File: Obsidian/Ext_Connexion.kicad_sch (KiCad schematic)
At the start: 36 parts, among them J4 Conn_02x20_Odd_Even

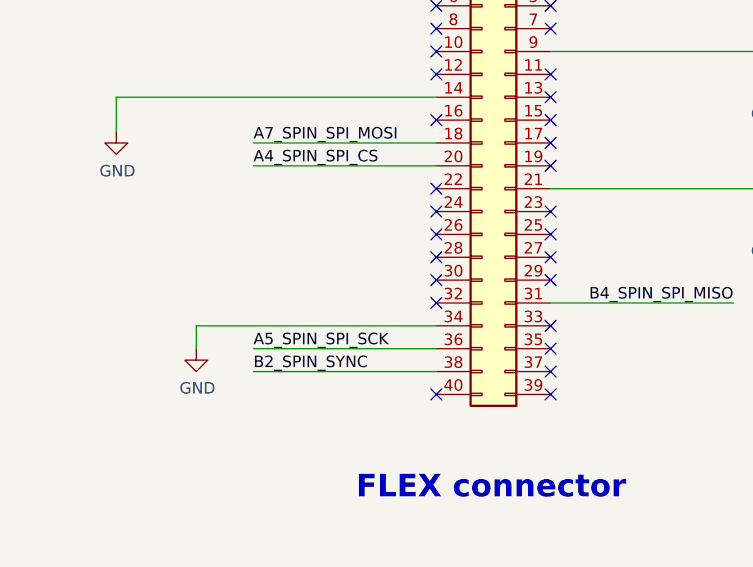
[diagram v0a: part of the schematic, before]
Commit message: moving flex pins for SCIN and SCK from PA13/PA14 to PC8/PC9
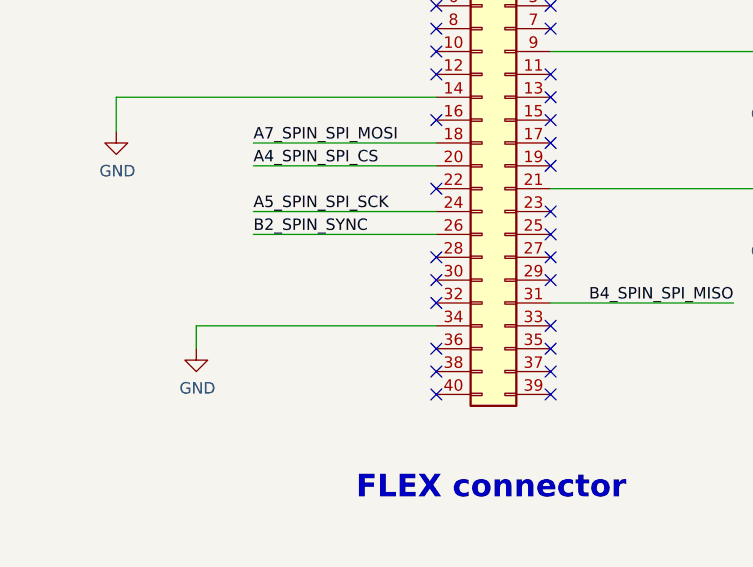
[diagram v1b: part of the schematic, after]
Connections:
- net A5_SPIN_SPI_SCK: now also J4.24 (Pin_24); no longer J4.36 (Pin_36)
- net B2_SPIN_SYNC: now also J4.26 (Pin_26); no longer J4.38 (Pin_38)
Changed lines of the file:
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@@
 	)
 	(no_connect
-		(at 58.42 153.67)
+		(at 58.42 168.91)
 	)
 	(no_connect
@@
 	)
 	(no_connect
-		(at 58.42 156.21)
-	)
-	(no_connect
 		(at 71.12 146.05)
 	)
@@
 	(no_connect
 		(at 71.12 130.81)
+	)
+	(no_connect
+		(at 58.42 171.45)
 	)
 	(no_connect
@@
 	(wire
 		(pts
-			(xy 38.1 168.91) (xy 58.42 168.91)
-		)
-		(stroke
-			(width 0)
-			(type default)
-		)
-	)
-	(wire
-		(pts
 			(xy 33.02 63.5) (xy 54.61 63.5)
 		)
@@
 	(wire
 		(pts
+			(xy 38.1 153.67) (xy 58.42 153.67)
+		)
+		(stroke
+			(width 0)
+			(type default)
+		)
+	)
+	(wire
+		(pts
 			(xy 142.24 44.45) (xy 160.02 44.45)
 		)
@@
 		(pts
 			(xy 38.1 146.05) (xy 58.42 146.05)
-		)
-		(stroke
-			(width 0)
-			(type default)
-		)
-	)
-	(wire
-		(pts
-			(xy 38.1 171.45) (xy 58.42 171.45)
 		)
 		(stroke
@@
 	(wire
 		(pts
+			(xy 38.1 156.21) (xy 58.42 156.21)
+		)
+		(stroke
+			(width 0)
+			(type default)
+		)
+	)
+	(wire
+		(pts
 			(xy 185.42 44.45) (xy 191.77 44.45)
 		)
@@
 		)
 	)
+	(label "A5_SPIN_SPI_SCK"
+		(at 38.1 153.67 0)
+		(effects
+			(font
+				(size 1.27 1.27)
+			)
+			(justify left bottom)
+		)
+	)
 	(label "ARDUINO_D13"
 		(at 146.05 72.39 0)
@@
 		)
 	)
+	(label "B2_SPIN_SYNC"
+		(at 38.1 156.21 0)
+		(effects
+			(font
+				(size 1.27 1.27)
+			)
+			(justify left bottom)
+		)
+	)
 	(label "{SPIN}"
 		(at 109.22 41.91 180)
@@
 		)
 	)
-	(label "B2_SPIN_SYNC"
-		(at 38.1 171.45 0)
-		(effects
-			(font
-				(size 1.27 1.27)
-			)
-			(justify left bottom)
-		)
-	)
 	(label "ARDUINO_D5"
 		(at 146.05 52.07 0)
@@
 		)
 	)
-	(label "A5_SPIN_SPI_SCK"
-		(at 38.1 168.91 0)
-		(effects
-			(font
-				(size 1.27 1.27)
-			)
-			(justify left bottom)
-		)
-	)

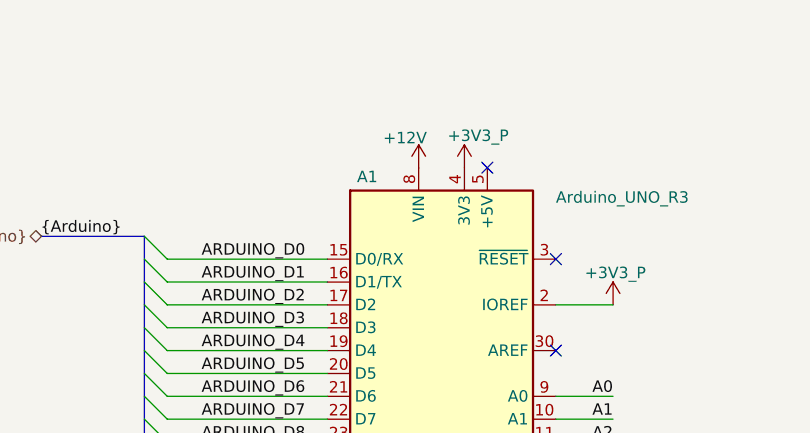
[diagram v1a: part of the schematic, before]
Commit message: correcting straightness of kicad plane around 1V2 regulator
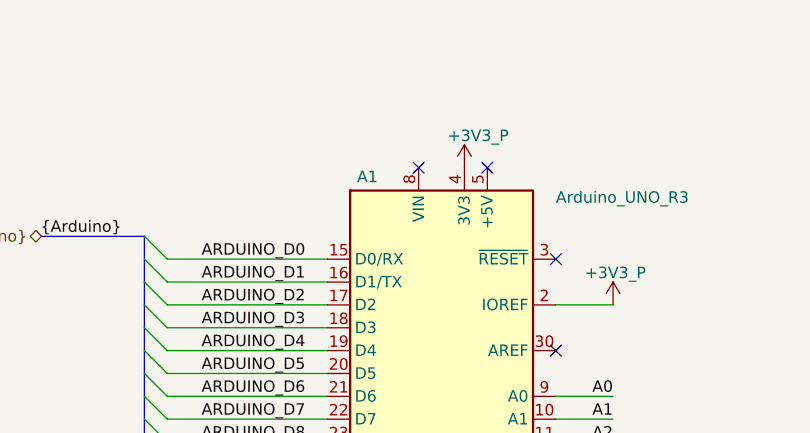
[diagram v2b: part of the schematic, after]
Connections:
- net +12V: no longer names the net of A1.8 (VIN)
- no-connect marks 34 -> 35
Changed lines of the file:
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@@
 	)
 	(no_connect
+		(at 170.18 29.21)
+	)
+	(no_connect
 		(at 71.12 140.97)
 	)
@@
 					(unit 1)
 				)
-			)
-		)
-	)
-	(symbol
-		(lib_id "Library_Symbol:+12V")
-		(at 170.18 29.21 0)
-		(unit 1)
-		(exclude_from_sim no)
-		(in_bom yes)
-		(on_board yes)
-		(dnp no)
-		(property "Reference" "#PWR0295"
-			(at 170.18 33.02 0)
-			(effects
-				(font
-					(size 1.27 1.27)
-				)
-				(hide yes)
-			)
-		)
-		(property "Value" "+12V"
-			(at 168.656 25.908 0)
-			(effects
-				(font
-					(size 1.27 1.27)
-				)
-			)
-		)
-		(property "Footprint" ""
-			(at 170.18 29.21 0)
-			(effects
-				(font
-					(size 1.27 1.27)
-				)
-				(hide yes)
-			)
-		)
-		(property "Datasheet" ""
-			(at 170.18 29.21 0)
-			(effects
-				(font
-					(size 1.27 1.27)
-				)
-				(hide yes)
-			)
-		)
-		(property "Description" "Power symbol creates a global label with name \"+12V\""
-			(at 170.18 29.21 0)
-			(effects
-				(font
-					(size 1.27 1.27)
-				)
-				(hide yes)
-			)
-		)
-		(pin "1"
-		)
-		(instances
-			(project "Obsidian"
-				(path "/c2a4f786-b14c-434a-acf7-b20fb2221b0b/37c76a7d-e360-409e-9f8e-819f870af943"
-					(reference "#PWR0295")
-					(unit 1)
-				)

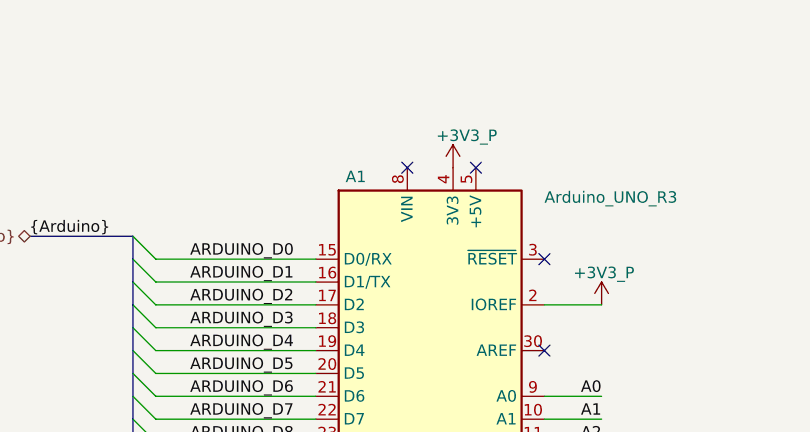
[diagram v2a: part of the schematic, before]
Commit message: Reconnecting 12V pins
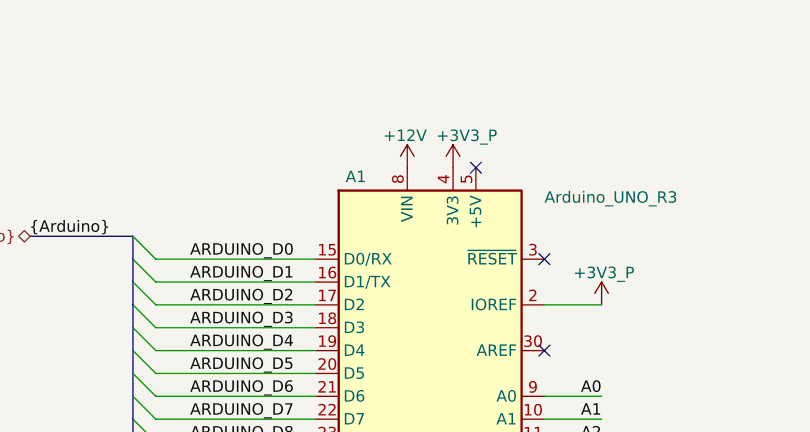
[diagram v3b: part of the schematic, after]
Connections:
- net +12V: now reaches A1.8 (VIN)
- no-connect marks 35 -> 34
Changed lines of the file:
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@@
 	)
 	(no_connect
-		(at 170.18 29.21)
-	)
-	(no_connect
 		(at 71.12 140.97)
 	)
@@
 					(unit 1)
 				)
+			)
+		)
+	)
+	(symbol
+		(lib_id "Library_Symbol:+12V")
+		(at 170.18 29.21 0)
+		(unit 1)
+		(exclude_from_sim no)
+		(in_bom yes)
+		(on_board yes)
+		(dnp no)
+		(property "Reference" "#PWR02"
+			(at 170.18 33.02 0)
+			(effects
+				(font
+					(size 1.27 1.27)
+				)
+				(hide yes)
+			)
+		)
+		(property "Value" "+12V"
+			(at 169.926 25.654 0)
+			(effects
+				(font
+					(size 1.27 1.27)
+				)
+			)
+		)
+		(property "Footprint" ""
+			(at 170.18 29.21 0)
+			(effects
+				(font
+					(size 1.27 1.27)
+				)
+				(hide yes)
+			)
+		)
+		(property "Datasheet" ""
+			(at 170.18 29.21 0)
+			(effects
+				(font
+					(size 1.27 1.27)
+				)
+				(hide yes)
+			)
+		)
+		(property "Description" "Power symbol creates a global label with name \"+12V\""
+			(at 170.18 29.21 0)
+			(effects
+				(font
+					(size 1.27 1.27)
+				)
+				(hide yes)
+			)
+		)
+		(pin "1"
+		)
+		(instances
+			(project "Obsidian"
+				(path "/c2a4f786-b14c-434a-acf7-b20fb2221b0b/37c76a7d-e360-409e-9f8e-819f870af943"
+					(reference "#PWR02")
+					(unit 1)
+				)

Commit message: adding production files, and documentations
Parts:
- J4: LCSC (none) -> C2763968
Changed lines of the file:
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@@
+			)
+		)
+		(property "LCSC" "C2763968"
+			(at 66.04 148.59 0)
+			(effects
+				(font
+					(size 1.27 1.27)
+				)
+				(hide yes)
 			)
 		)

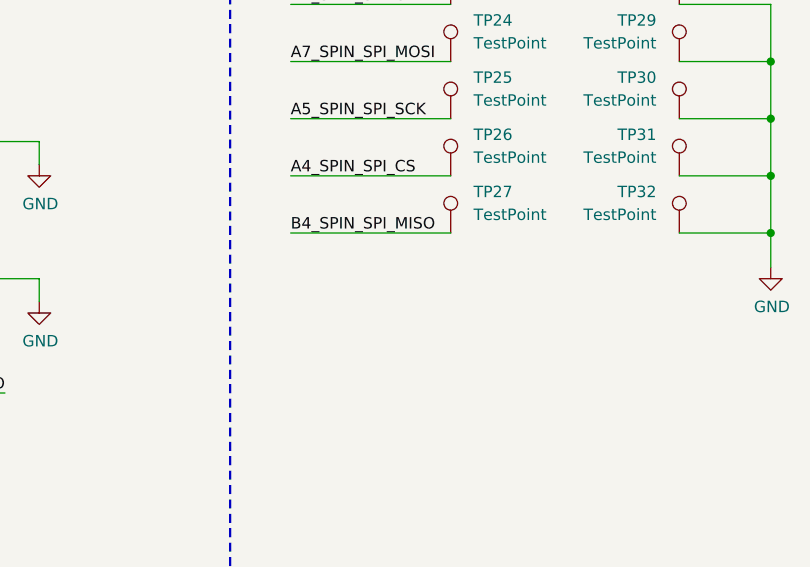
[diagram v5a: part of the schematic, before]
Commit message: Adding documentation for configuration with flash memory, adding more comments to schematic
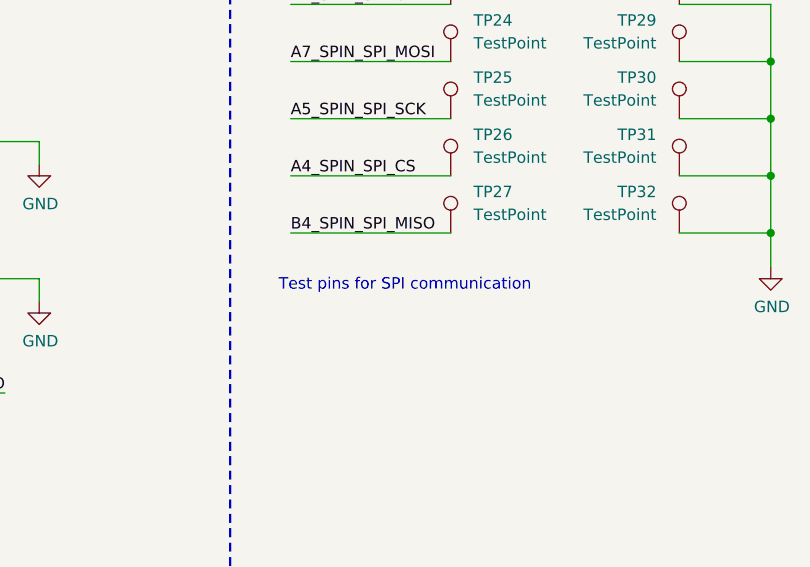
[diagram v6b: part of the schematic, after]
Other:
- note added: "Test pins for SPI communication"
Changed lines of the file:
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@@
+		)
+	)
+	(text "Test pins for SPI communication"
+		(exclude_from_sim no)
+		(at 135.89 151.892 0)
+		(effects
+			(font
+				(face "Arial")
+				(size 1.27 1.27)
+			)
 		)
 	)

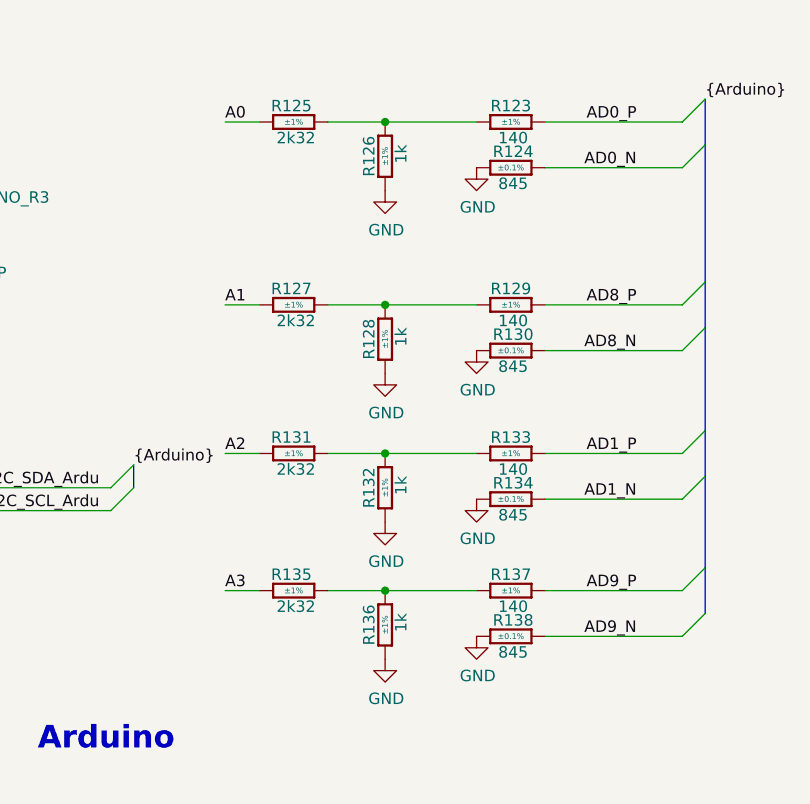
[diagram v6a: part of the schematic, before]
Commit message: Cleaning symbol fields
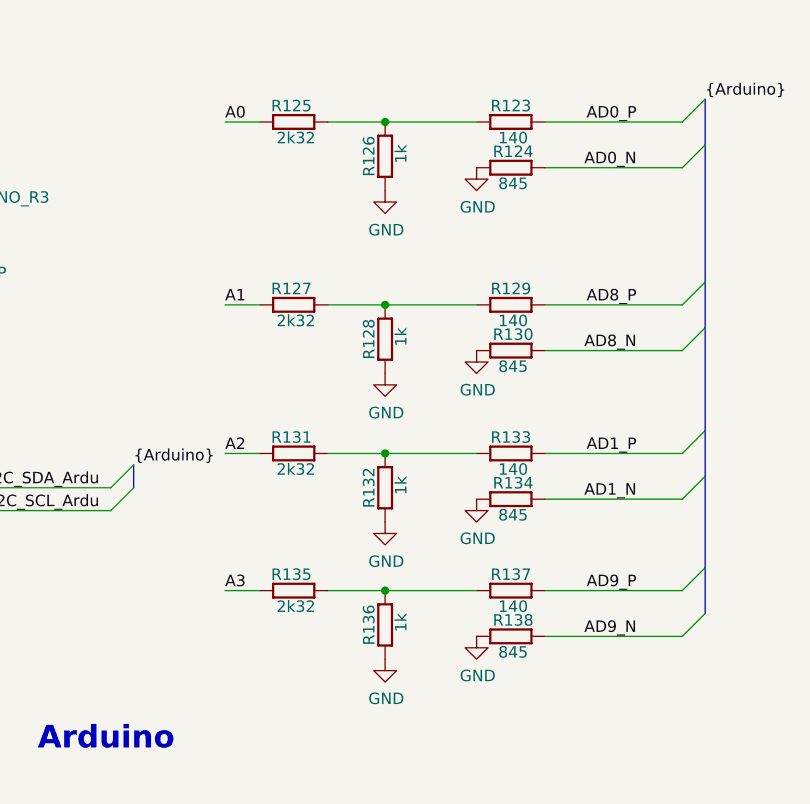
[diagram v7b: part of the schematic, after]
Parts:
- A1: Component Class STACKED_SHIELD -> (none)
- R123, R129, R133, R137: Author CERN DEM BC -> (none); Case 0402 -> (none); Comment 140 -> (none); Component Kind Standard -> (none); Component Type Standard -> (none); ComponentHeight (none) -> (none); CreateDate 07/29/15 00:00:00 -> (none); Database Table Name Resistors -> (none); Footprint Library Resistors SMD -> (none); Footprint Path PcbLib\Resistors SMD.PcbLib -> (none); Footprint Ref RESC1005X40N -> (none); HelpURL \\cern.ch\dfs\Applications\Altium\Datasheets\R0402_Phycomp_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 -> (none); LatestRevisionDate 07/29/15 00:00:00 -> (none); Library Name Resistors SMD -> (none); Library Path SchLib\Resistors.SchLib -> (none); Library Ref Resistor - 1% -> (none); License CC-BY-SA 4.0 -> (none); Manufacturer GENERIC -> (none); Manufacturer Part Number R0402_140R_1%_0.0625W_100PPM -> (none); Manufacturer1 ComponentHeight 0.4mm -> (none); Manufacturer1 Example YAGEO PHYCOMP -> (none); Manufacturer1 Part Number 232270671401L or RC0402FR-07140RL -> (none); Mounted Yes -> (none); PackageDescription (none) -> (none); Part Description General Purpose Thick Film Chip Resistor -> (none); Part Number R0402_140R_1%_0.0625W_100PPM -> (none); Pin Count 2 -> (none); Power 0.0625W -> (none); PressFit No -> (none); SMD Yes -> (none); Sense No -> (none); Sense Comment (none) -> (none); Socket No -> (none); Status Not Recommended -> (none); Status Comment (none) -> (none); TC ±100ppm/°C -> (none); Tolerance ±1% -> (none); Voltage (none) -> (none)
- R124, R130, R134, R138: Author CERN DEM HF -> (none); Case 0402 -> (none); Comment 845 -> (none); Component Kind Standard -> (none); Component Type Standard -> (none); ComponentHeight (none) -> (none); CreateDate 05/25/23 00:00:00 -> (none); Database Table Name Resistors -> (none); Footprint Library Resistors SMD -> (none); Footprint Path PcbLib\Resistors SMD.PcbLib -> (none); Footprint Ref RESC1005X40N -> (none); HelpURL \\cern.ch\dfs\Applications\Altium\Datasheets\R0402_TYCO_CPF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 -> (none); LatestRevisionDate 05/25/23 00:00:00 -> (none); Library Name Resistors SMD -> (none); Library Path SchLib\Resistors.SchLib -> (none); Library Ref Resistor - 0.1% -> (none); License CC-BY-SA 4.0 -> (none); Manufacturer GENERIC -> (none); Manufacturer Part Number R0402_845R_0.1%_0.063W_25PPM -> (none); Manufacturer1 ComponentHeight 0.4mm -> (none); Manufacturer1 Example TE CONNECTIVITY -> (none); Mounted Yes -> (none); PackageDescription (none) -> (none); Part Description Thin Film Precision Resistor -> (none); Part Number R0402_845R_0.1%_0.063W_25PPM -> (none); Pin Count 2 -> (none); Power 0.063W -> (none); PressFit No -> (none); SMD Yes -> (none); Sense No -> (none); Sense Comment (none) -> (none); Socket No -> (none); Status Not Recommended -> (none); Status Comment (none) -> (none); TC ±25ppm/°C -> (none); Tolerance ±0.1% -> (none); Voltage (none) -> (none)
- R125, R127, R131, R135: Author CERN DEM JLC -> (none); Case 0402 -> (none); Comment 2k -> (none); Component Kind Standard -> (none); Component Type Standard -> (none); ComponentHeight (none) -> (none); CreateDate 12/03/07 00:00:00 -> (none); Database Table Name Resistors -> (none); Footprint Library Resistors SMD -> (none); Footprint Path PcbLib\Resistors SMD.PcbLib -> (none); Footprint Ref RESC1005X40N -> (none); HelpURL \\cern.ch\dfs\Applications\Altium\Datasheets\R0402_Phycomp_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 -> (none); LatestRevisionDate 10/17/12 00:00:00 -> (none); Library Name Resistors SMD -> (none); Library Path SchLib\Resistors.SchLib -> (none); Library Ref Resistor - 1% -> (none); License CC-BY-SA 4.0 -> (none); Manufacturer GENERIC -> (none); Manufacturer Part Number R0402_2K32_1%_0.0625W_100PPM -> (none); Manufacturer1 ComponentHeight 0.4mm -> (none); Manufacturer1 Example YAGEO PHYCOMP -> (none); Mounted Yes -> (none); PackageDescription (none) -> (none); Part Description General Purpose Thick Film Chip Resistor -> (none); Part Number R0402_2K32_1%_0.0625W_100PPM -> (none); Pin Count 2 -> (none); Power 0.0625W -> (none); PressFit No -> (none); SMD Yes -> (none); Sense No -> (none); Sense Comment (none) -> (none); Socket No -> (none); Status Not Recommended -> (none); Status Comment (none) -> (none); TC ±100ppm/°C -> (none); Tolerance ±1% -> (none); Voltage (none) -> (none)
- R126, R128, R132, R136: Author CERN DEM JLC -> (none); Case 0402 -> (none); Comment 1k -> (none); Component Kind Standard -> (none); Component Type Standard -> (none); ComponentHeight (none) -> (none); CreateDate 12/03/07 00:00:00 -> (none); Database Table Name Resistors -> (none); Footprint Library Resistors SMD -> (none); Footprint Path PcbLib\Resistors SMD.PcbLib -> (none); Footprint Ref RESC1005X40N -> (none); HelpURL \\cern.ch\dfs\Applications\Altium\Datasheets\R0402_Phycomp_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 -> (none); LatestRevisionDate 10/17/12 00:00:00 -> (none); Library Name Resistors SMD -> (none); Library Path SchLib\Resistors.SchLib -> (none); Library Ref Resistor - 1% -> (none); License CC-BY-SA 4.0 -> (none); Manufacturer GENERIC -> (none); Manufacturer Part Number R0402_1K_1%_0.0625W_100PPM -> (none); Manufacturer1 ComponentHeight 0.4mm -> (none); Manufacturer1 Example YAGEO PHYCOMP -> (none); Manufacturer1 Part Number 232270671002L -> (none); Mounted Yes -> (none); PackageDescription (none) -> (none); Part Description General Purpose Thick Film Chip Resistor -> (none); Part Number R0402_1K_1%_0.0625W_100PPM -> (none); Pin Count 2 -> (none); Power 0.0625W -> (none); PressFit No -> (none); SMD Yes -> (none); Sense No -> (none); Sense Comment (none) -> (none); Socket No -> (none); Status Not Recommended -> (none); Status Comment (none) -> (none); TC ±100ppm/°C -> (none); Tolerance ±1% -> (none); Voltage (none) -> (none)
